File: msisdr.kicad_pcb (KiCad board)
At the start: 2 copper layers, 46.3 x 90.7 mm, 76 parts, among them J1 VCC_GPIO, J10 SMA_VHF1, J11 USB_OTG, J2 GPIO0, J3 GPIO1, J4 GPIO2, J5 GPIO3, J6 SMA_0_30MHZ, J7 SMA_30_60MHZ, J8 SMA_VHF2, J9 SMA_UHF, U1 msi2500, U2 msi001, U3 RT9193-28, U4 XC6206P302MR, Y1 24MHz, Y2 24MHZ

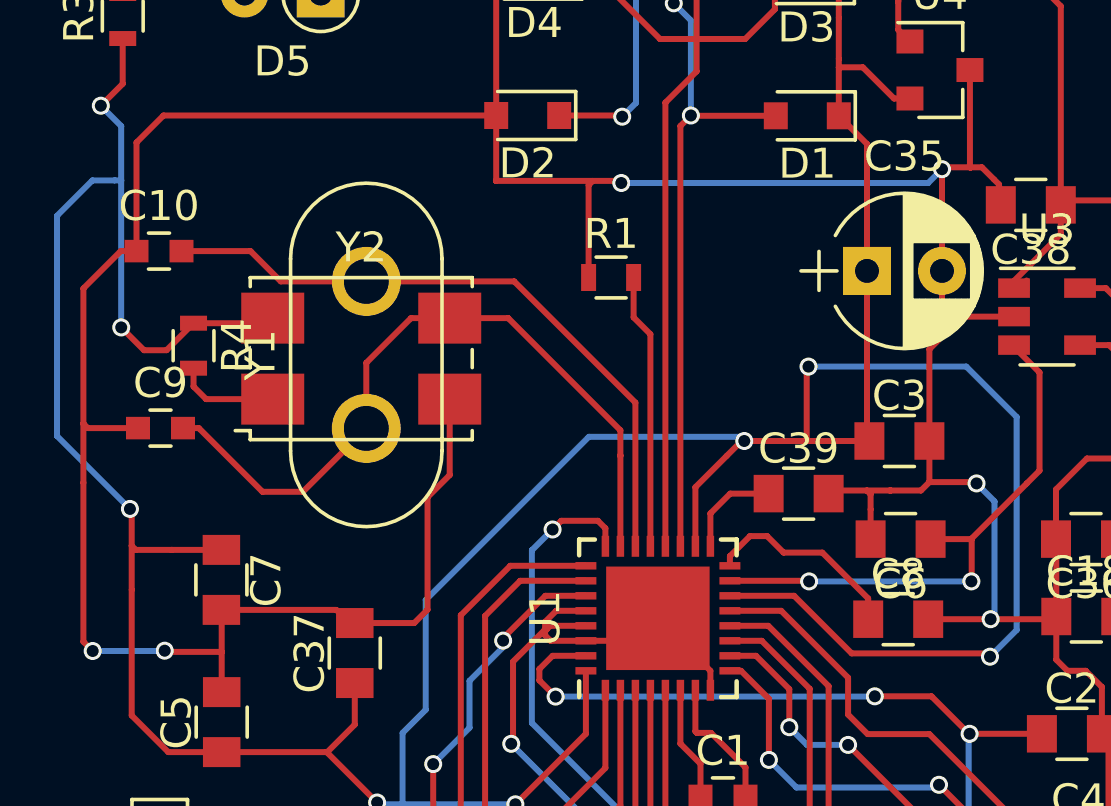
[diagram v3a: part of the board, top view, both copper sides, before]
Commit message: fix oscillator connect to x1 error
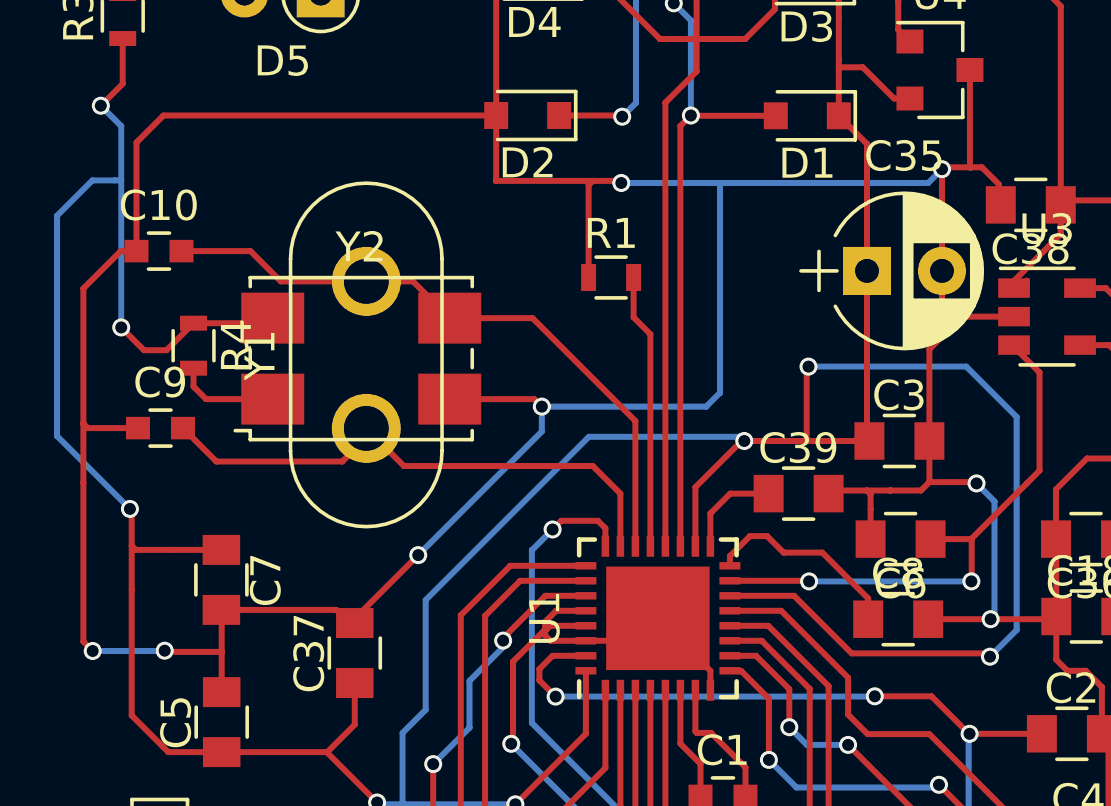
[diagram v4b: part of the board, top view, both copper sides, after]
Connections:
- Y2 pad 3: Net-(C9-Pad2) -> Net-(C10-Pad2)
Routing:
- net GND: track 420.5 -> 436.6 mm, vias 18 -> 20
- net Net-(C9-Pad2): track 24.6 -> 18.3 mm
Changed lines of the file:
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@@
     (thickness 1.6)
     (drawings 5)
-    (tracks 905)
+    (tracks 910)
     (zones 0)
     (modules 76)
@@
       (net 34 GND))
     (pad 3 smd rect (at 2.95 -1.35) (size 2.1 1.7) (layers F.Cu F.Paste F.Mask)
-      (net 7 "Net-(C9-Pad2)"))
+      (net 42 "Net-(C10-Pad2)"))
     (pad 4 smd rect (at -2.95 -1.35) (size 2.1 1.7) (layers F.Cu F.Paste F.Mask)
       (net 4 VDIG))
@@
   (segment (start 140.549 75.316) (end 140.569 75.336) (width 0.2) (layer F.Cu) (net 6))
   (segment (start 145.989 73.926) (end 144.619 73.926) (width 0.2) (layer F.Cu) (net 6))
-  (segment (start 119.699 70.226) (end 120.226 70.226) (width 0.2) (layer F.Cu) (net 7))
-  (segment (start 123.695 72.35) (end 125.809 70.236) (width 0.2) (layer F.Cu) (net 7))
-  (segment (start 122.35 72.35) (end 123.695 72.35) (width 0.2) (layer F.Cu) (net 7))
-  (segment (start 120.226 70.226) (end 122.35 72.35) (width 0.2) (layer F.Cu) (net 7))
-  (segment (start 128.59 66.56) (end 127.3 66.56) (width 0.2) (layer F.Cu) (net 7))
-  (segment (start 125.809 68.051) (end 125.809 70.236) (width 0.2) (layer F.Cu) (net 7))
-  (segment (start 127.3 66.56) (end 125.809 68.051) (width 0.2) (layer F.Cu) (net 7))
-  (segment (start 134.279 71.15) (end 134.279 70.299) (width 0.2) (layer F.Cu) (net 7))
-  (segment (start 130.54 66.56) (end 128.59 66.56) (width 0.2) (layer F.Cu) (net 7))
-  (segment (start 134.279 70.299) (end 130.54 66.56) (width 0.2) (layer F.Cu) (net 7))
-  (segment (start 134.279 74.166) (end 134.279 71.15) (width 0.2) (layer F.Cu) (net 7))
-  (segment (start 134.279 71.15) (end 134.279 71.126) (width 0.2) (layer F.Cu) (net 7))
+  (segment (start 134.279 74.166) (end 134.279 72.409) (width 0.2) (layer F.Cu) (net 7) (status 400000))
+  (segment (start 127.063 71.49) (end 125.809 70.236) (width 0.2) (layer F.Cu) (net 7) (status 800000))
+  (segment (start 133.36 71.49) (end 127.063 71.49) (width 0.2) (layer F.Cu) (net 7))
+  (segment (start 134.279 72.409) (end 133.36 71.49) (width 0.2) (layer F.Cu) (net 7))
+  (segment (start 125.809 70.236) (end 125.809 70.541) (width 0.2) (layer F.Cu) (net 7))
+  (segment (start 125.809 70.541) (end 125.01 71.34) (width 0.2) (layer F.Cu) (net 7))
+  (segment (start 120.813 71.34) (end 119.699 70.226) (width 0.2) (layer F.Cu) (net 7))
+  (segment (start 125.01 71.34) (end 120.813 71.34) (width 0.2) (layer F.Cu) (net 7))
   (segment (start 125.799 70.226) (end 125.809 70.236) (width 0.2) (layer F.Cu) (net 7))
   (segment (start 150.799 73.926) (end 152.264 73.926) (width 0.2) (layer F.Cu) (net 8))
@@
   (segment (start 123.09094 123.64208) (end 126.36762 123.64208) (width 0.2) (layer F.Cu) (net 33))
   (segment (start 126.36762 123.64208) (end 126.7968 123.2129) (width 0.2) (layer F.Cu) (net 33))
-  (segment (start 147.4 66.51) (end 145.038 66.51) (width 0.2) (layer F.Cu) (net 34) (status 400000))
+  (segment (start 137.6 62.056) (end 137.6 69.05) (width 0.2) (layer B.Cu) (net 34))
+  (segment (start 137.14 69.51) (end 131.66 69.51) (width 0.2) (layer B.Cu) (net 34))
+  (segment (start 137.6 69.05) (end 137.14 69.51) (width 0.2) (layer B.Cu) (net 34))
+  (segment (start 125.4252 76.724) (end 125.4252 76.5748) (width 0.2) (layer F.Cu) (net 34) (status C00000))
+  (segment (start 125.4252 76.5748) (end 127.54 74.46) (width 0.2) (layer F.Cu) (net 34) (status 400000))
+  (segment (start 131.66 70.34) (end 131.66 69.51) (width 0.2) (layer B.Cu) (net 34))
+  (segment (start 127.54 74.46) (end 131.66 70.34) (width 0.2) (layer B.Cu) (net 34))
+  (via (at 127.54 74.46) (size 0.6) (drill 0.4) (layers F.Cu B.Cu) (net 34))
+  (segment (start 131.41 69.26) (end 128.59 69.26) (width 0.2) (layer F.Cu) (net 34) (status 800000))
+  (segment (start 131.66 69.51) (end 131.41 69.26) (width 0.2) (layer F.Cu) (net 34))
+  (via (at 131.66 69.51) (size 0.6) (drill 0.4) (layers F.Cu B.Cu) (net 34))
+  (segment (start 147.4 66.51) (end 145.038 66.51) (width 0.2) (layer F.Cu) (net 34))
   (segment (start 145.038 66.51) (end 144.999 66.471) (width 0.2) (layer F.Cu) (net 34))
   (segment (start 131.7825 76.9725) (end 131.7375 76.9725) (width 0.2) (layer F.Cu) (net 34))
@@
   (segment (start 130.349 55.126) (end 124.904 55.126) (width 0.2) (layer F.Cu) (net 34))
   (segment (start 124.904 55.126) (end 124.29 55.74) (width 0.2) (layer F.Cu) (net 34))
-  (segment (start 128.59 69.26) (end 128.59 71.79) (width 0.2) (layer F.Cu) (net 34))
-  (segment (start 127.406 76.724) (end 125.4252 76.724) (width 0.2) (layer F.Cu) (net 34))
-  (segment (start 127.85 76.28) (end 127.406 76.724) (width 0.2) (layer F.Cu) (net 34))
-  (segment (start 127.85 72.53) (end 127.85 76.28) (width 0.2) (layer F.Cu) (net 34))
-  (segment (start 128.59 71.79) (end 127.85 72.53) (width 0.2) (layer F.Cu) (net 34))
   (segment (start 142.619 72.936) (end 142.619 72.429) (width 0.2) (layer F.Cu) (net 34))
   (segment (start 142.619 73.926) (end 142.619 72.936) (width 0.2) (layer F.Cu) (net 34))
@@
   (segment (start 134.309 62.056) (end 134.239 61.986) (width 0.2) (layer F.Cu) (net 34))
   (via (at 134.309 62.056) (size 0.6) (drill 0.4) (layers F.Cu B.Cu) (net 34))
-  (segment (start 144.539 62.056) (end 134.309 62.056) (width 0.2) (layer B.Cu) (net 34))
+  (segment (start 144.539 62.056) (end 137.6 62.056) (width 0.2) (layer B.Cu) (net 34))
+  (segment (start 137.6 62.056) (end 134.309 62.056) (width 0.2) (layer B.Cu) (net 34))
   (segment (start 144.539 62.056) (end 144.999 61.596) (width 0.2) (layer B.Cu) (net 34))
   (segment (start 144.999 64.986) (end 145.039 64.986) (width 0.2) (layer F.Cu) (net 34))
@@
   (segment (start 141.009 74.376) (end 139.719 74.376) (width 0.2) (layer F.Cu) (net 41))
   (segment (start 142.539 75.906) (end 141.009 74.376) (width 0.2) (layer F.Cu) (net 41))
-  (segment (start 125.809 65.336) (end 130.739 65.336) (width 0.2) (layer F.Cu) (net 42))
-  (segment (start 134.779 69.376) (end 134.779 74.166) (width 0.2) (layer F.Cu) (net 42))
-  (segment (start 130.739 65.336) (end 134.779 69.376) (width 0.2) (layer F.Cu) (net 42))
+  (segment (start 128.59 66.56) (end 131.35 66.56) (width 0.2) (layer F.Cu) (net 42))
+  (segment (start 134.779 69.989) (end 134.779 74.166) (width 0.2) (layer F.Cu) (net 42))
+  (segment (start 131.35 66.56) (end 134.779 69.989) (width 0.2) (layer F.Cu) (net 42))
+  (segment (start 125.809 65.336) (end 127.366 65.336) (width 0.2) (layer F.Cu) (net 42))
+  (segment (start 127.366 65.336) (end 128.59 66.56) (width 0.2) (layer F.Cu) (net 42))
   (segment (start 119.649 64.326) (end 121.949 64.326) (width 0.2) (layer F.Cu) (net 42))
   (segment (start 122.959 65.336) (end 125.809 65.336) (width 0.2) (layer F.Cu) (net 42))

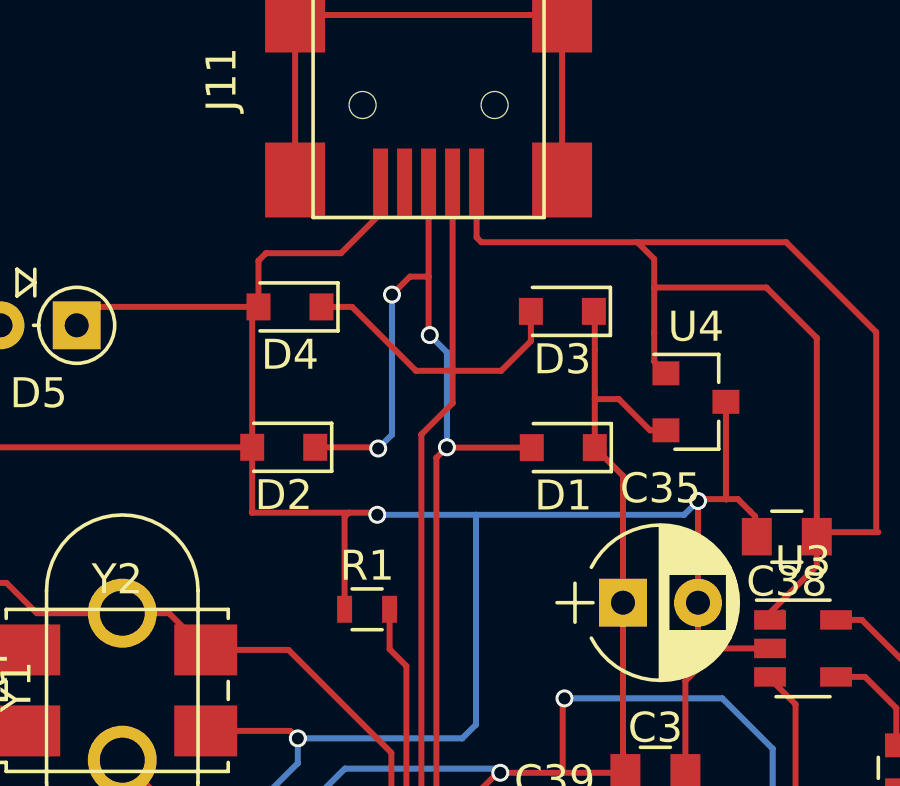
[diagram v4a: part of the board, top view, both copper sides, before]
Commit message: use bav99 replace diode
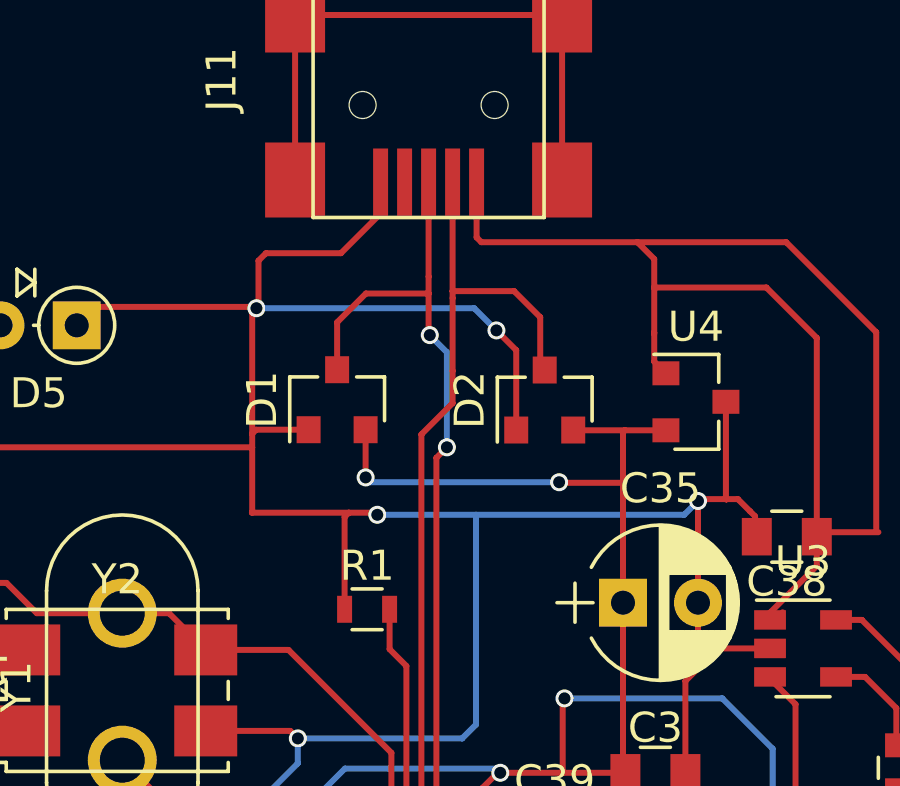
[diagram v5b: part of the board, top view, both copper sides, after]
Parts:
- removed D3, D4: D, Diodes_SMD:D_0805
- D1, D2: value D -> BAV99LT1G; footprint Diodes_SMD:D_0805 -> TO_SOT_Packages_SMD:SOT-23
- moved D2 8.84 mm to (139.9, 58.2), turned to 90 degrees
- moved D1 7.71 mm to (133.0, 58.2), turned to 90 degrees
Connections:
- D1 pad 1: VDIG -> GND
- D1 pad 2: USB_DP -> VDIG
- D2 pad 1: USB_DP -> GND
- D2 pad 2: GND -> VDIG
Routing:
- net GND: track 436.6 -> 450.6 mm, vias 20 -> 22
- net USB_DP: track 35.3 -> 28.6 mm, vias 4 -> 2
- net VDIG: track 136.6 -> 142.8 mm, vias 8 -> 10
- net USB_DM: track 32.9 -> 28.7 mm

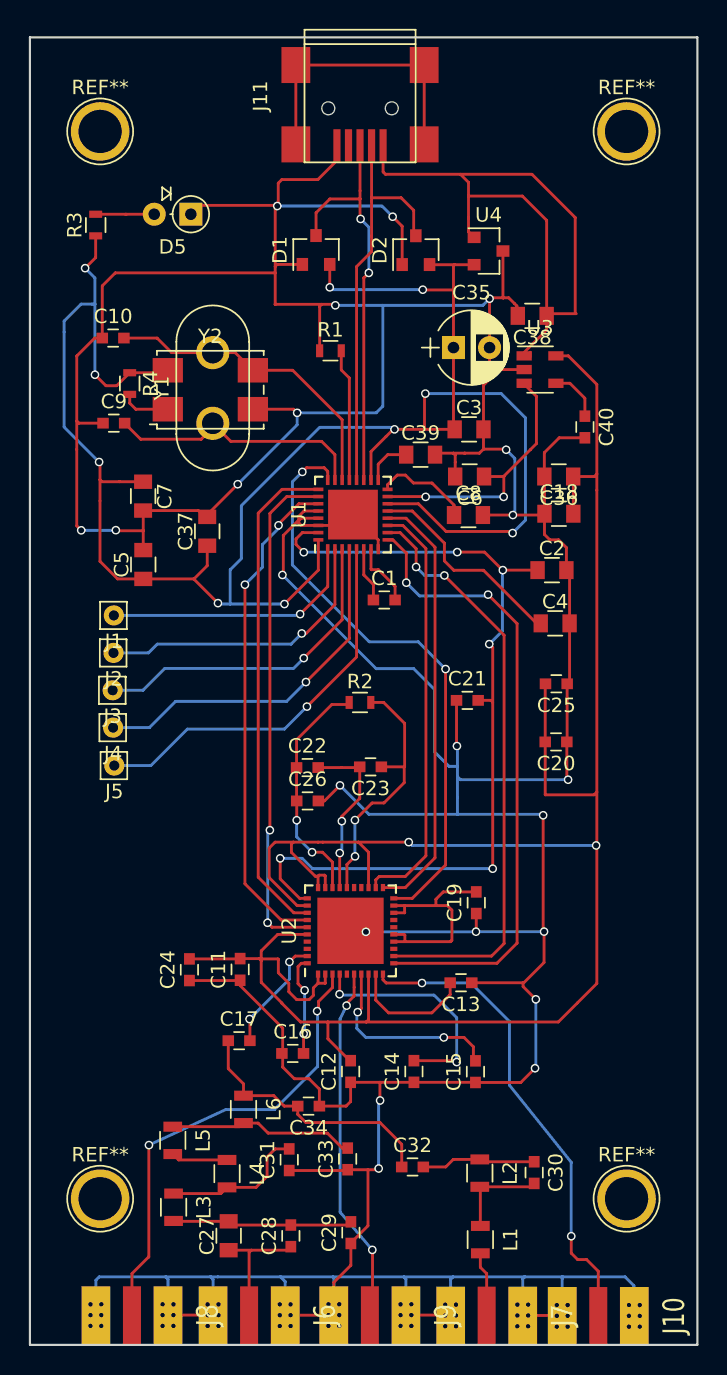
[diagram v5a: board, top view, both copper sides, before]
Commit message: add gpio pull down res
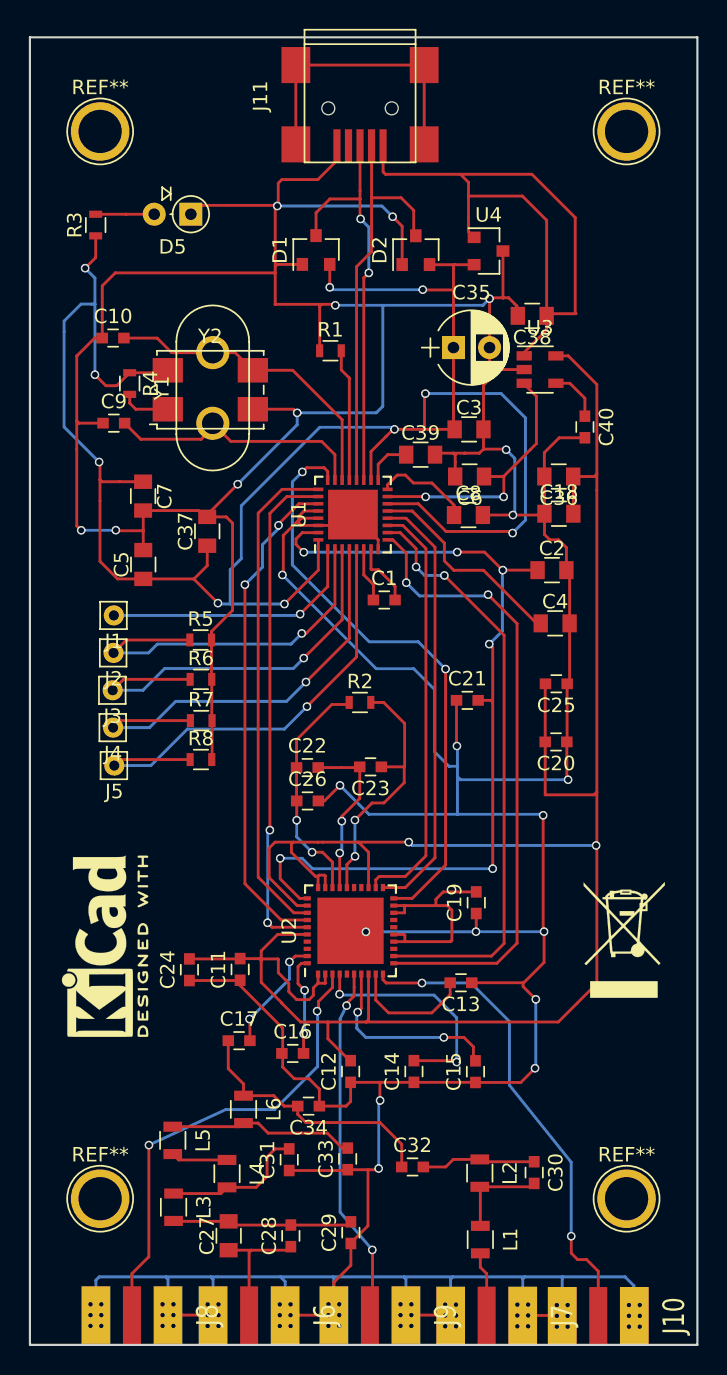
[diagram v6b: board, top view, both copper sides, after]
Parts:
- added R5: 10K, Resistors_SMD:R_0603, F.Cu at (125.0, 85.3)
- added R6: 10K, Resistors_SMD:R_0603, F.Cu at (125.0, 88.0)
- added R7: 10K, Resistors_SMD:R_0603, F.Cu at (125.0, 90.8)
- added R8: 10K, Resistors_SMD:R_0603, F.Cu at (125.0, 93.5)
- added REF***: KiCad-Logo2_6mm_SilkScreen, Symbols:KiCad-Logo2_6mm_SilkScreen, F.Cu at (118.3, 106.5)
- added REF***: WEEE-Logo_5.6x8mm_SilkScreen, Symbols:WEEE-Logo_5.6x8mm_SilkScreen, F.Cu at (154.3, 106.1)
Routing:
- net GND: track 450.6 -> 469.5 mm
- net Net-(J3-Pad1): track 22.8 -> 28.5 mm
- net Net-(J2-Pad1): track 20.6 -> 26.3 mm
- net Net-(J4-Pad1): track 25.1 -> 30.7 mm
- net Net-(J5-Pad1): track 27.4 -> 32.8 mm

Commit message: pcb version 2
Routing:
- added copper zone on B.Cu, net GND
- added copper zone on F.Cu, net GND
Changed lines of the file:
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@@
     (area 113.056599 43.399639 159.490481 134.207321)
     (thickness 1.6)
-    (drawings 5)
+    (drawings 7)
     (tracks 937)
     (zones 0)
@@
   (layers
     (0 F.Cu signal)
-    (31 B.Cu signal)
+    (31 B.Cu signal hide)
     (32 B.Adhes user)
     (33 F.Adhes user)
@@
       (xy 2.823256 -3.900663)) (layer F.SilkS) (width 0.01))
   )
+  (dimension 90.680001 (width 0.3) (layer Eco2.User)
+    (gr_text "90.680 mm" (at 165.655348 88.789311 270.0063185) (layer Eco2.User)
+      (effects (font (size 1.5 1.5) (thickness 0.3)))
+    )
+    (feature1 (pts (xy 159.41 134.13) (xy 167.010348 134.129162)))
+    (feature2 (pts (xy 159.4 43.45) (xy 167.000348 43.449162)))
+    (crossbar (pts (xy 164.300348 43.44946) (xy 164.310348 134.12946)))
+    (arrow1a (pts (xy 164.310348 134.12946) (xy 163.723803 133.003021)))
+    (arrow1b (pts (xy 164.310348 134.12946) (xy 164.896645 133.002892)))
+    (arrow2a (pts (xy 164.300348 43.44946) (xy 163.714051 44.576028)))
+    (arrow2b (pts (xy 164.300348 43.44946) (xy 164.886893 44.575899)))
+  )
+  (dimension 46.260001 (width 0.3) (layer Eco2.User)
+    (gr_text "46.260 mm" (at 136.269129 39.445068 0.01238559849) (layer Eco2.User)
+      (effects (font (size 1.5 1.5) (thickness 0.3)))
+    )
+    (feature1 (pts (xy 159.4 43.47) (xy 159.398837 38.090068)))
+    (feature2 (pts (xy 113.14 43.48) (xy 113.138837 38.100068)))
+    (crossbar (pts (xy 113.139421 40.800068) (xy 159.399421 40.790068)))
+    (arrow1a (pts (xy 159.399421 40.790068) (xy 158.273044 41.376732)))
+    (arrow1b (pts (xy 159.399421 40.790068) (xy 158.272791 40.203891)))
+    (arrow2a (pts (xy 113.139421 40.800068) (xy 114.266051 41.386245)))
+    (arrow2b (pts (xy 113.139421 40.800068) (xy 114.265798 40.213404)))
+  )
   (gr_line (start 159.41548 134.13232) (end 113.13668 134.13232) (angle 90) (layer Edge.Cuts) (width 0.15))
   (gr_line (start 113.1316 134.08914) (end 113.157 134.08914) (angle 90) (layer Edge.Cuts) (width 0.15))
@@
   (segment (start 120.05 68.84) (end 120.05 68.23) (width 0.2) (layer F.Cu) (net 63))
   (segment (start 120.47 69.26) (end 120.05 68.84) (width 0.2) (layer F.Cu) (net 63))
+  (zone (net 34) (net_name GND) (layer F.Cu) (hatch edge 0.508)
+    (connect_pads (clearance 0.508))
+    (min_thickness 0.254)
+    (fill yes (arc_segments 16) (thermal_gap 0.508) (thermal_bridge_width 0.508))
+    (polygon
+      (pts
+        (xy 113.21 43.45) (xy 159.38 43.5) (xy 159.42 134.14) (xy 113.16 134.13)
+      )
+    )
+  )
+  (zone (net 34) (net_name GND) (layer B.Cu) (hatch edge 0.508)
+    (connect_pads (clearance 0.508))
+    (min_thickness 0.254)
+    (fill yes (arc_segments 16) (thermal_gap 0.508) (thermal_bridge_width 0.508))
+    (polygon
+      (pts
+        (xy 113.17 43.49) (xy 159.38 43.48) (xy 159.41 134.13) (xy 113.14 134.13)
+      )
+    )
+  )
 )
